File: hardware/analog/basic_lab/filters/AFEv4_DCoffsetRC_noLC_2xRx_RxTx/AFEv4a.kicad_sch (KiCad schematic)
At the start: 17 parts, among them J1 Connector_Generic_Conn_01x20, J2 Connector_Generic_Conn_01x02, J3 Connector_Generic_Conn_01x02, J4 Connector_Generic_Conn_01x02, J5 Connector_Generic_Conn_01x02, J6 Connector_Generic_Conn_01x02

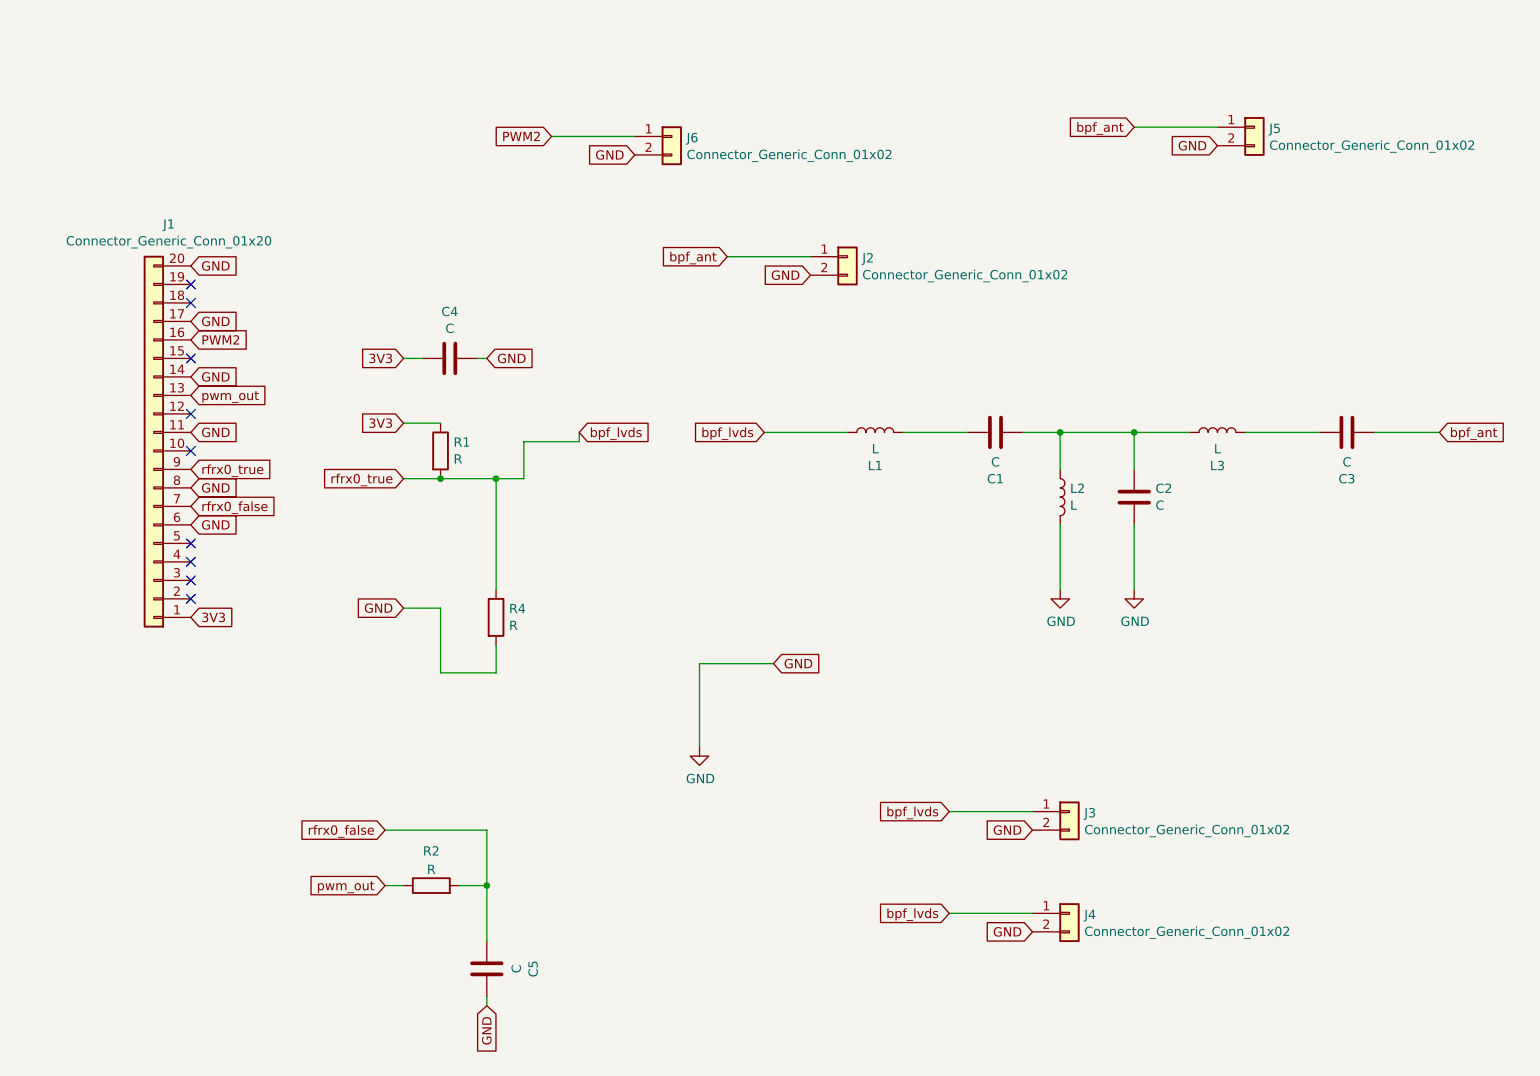
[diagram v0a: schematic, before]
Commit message: started 2xRx / RxTx PCBs with no / simple LC filters
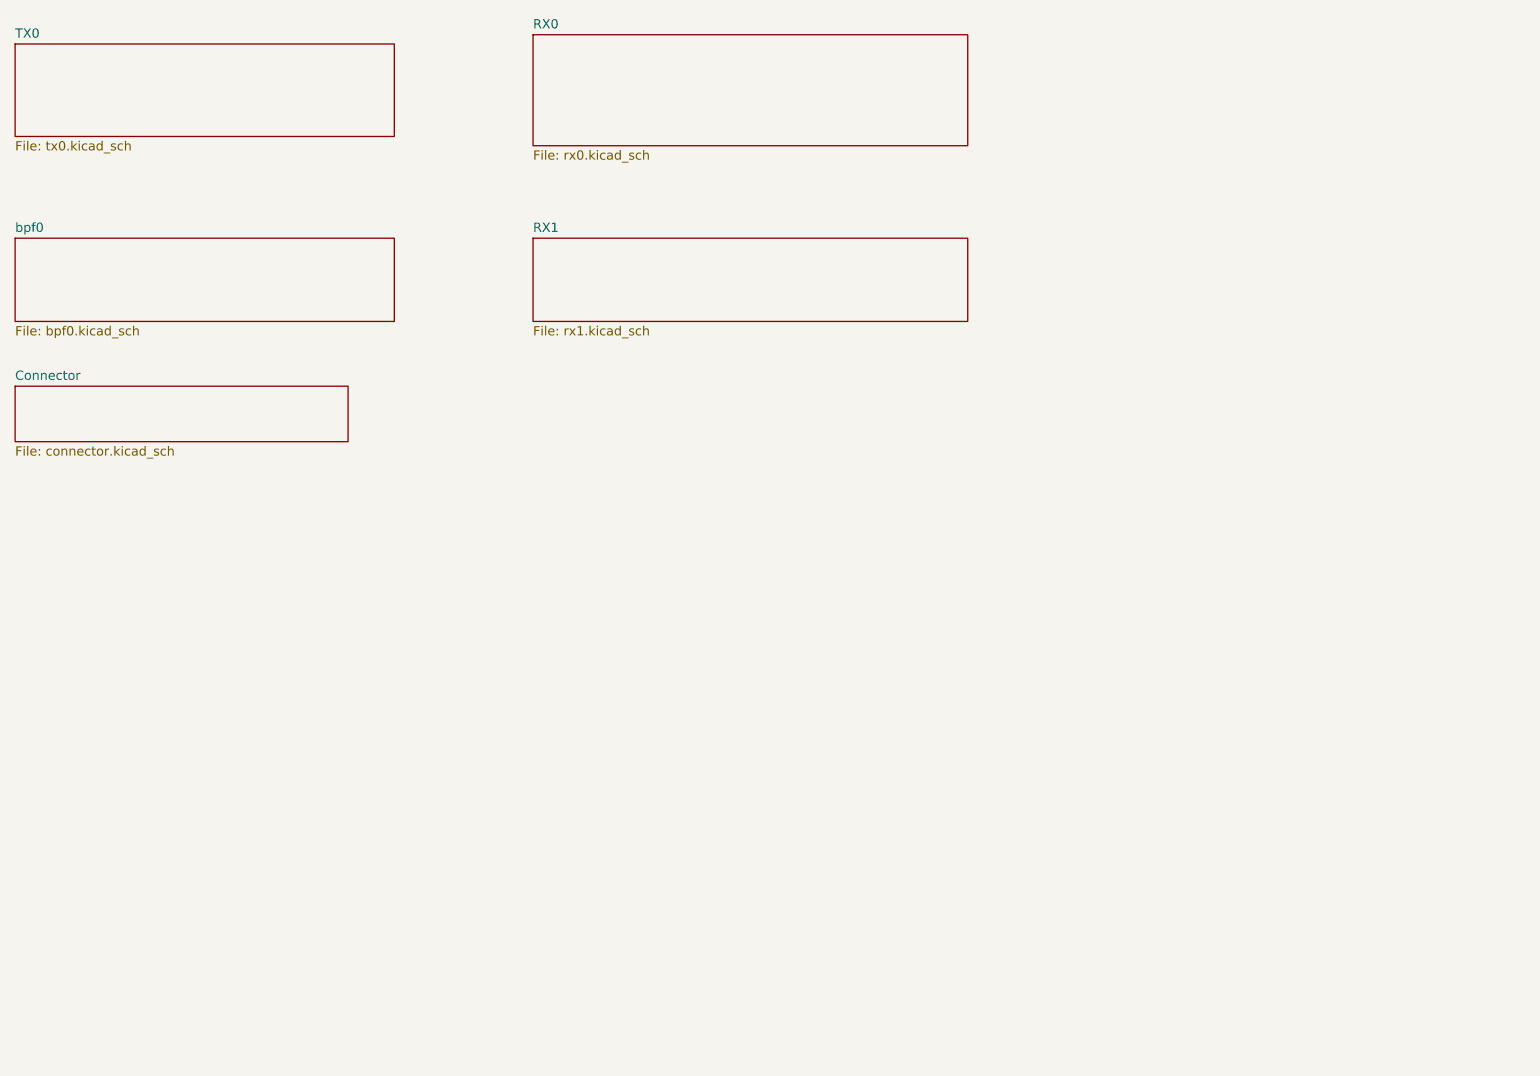
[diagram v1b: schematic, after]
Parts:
- removed C1, C2, C3, C4, C5: C, Capacitor_THT:C_Axial_L3.8mm_D2.6mm_P7.50mm_Horizontal, symbol Device:C
- removed J1: Connector_Generic_Conn_01x20, Connector_PinHeader_2.54mm:PinHeader_1x20_P2.54mm_Vertical, symbol bgt:Connector_Generic_Conn_01x20
- removed J2, J3, J4, J5, J6: Connector_Generic_Conn_01x02, Connector_PinHeader_2.54mm:PinHeader_1x02_P2.54mm_Vertical, symbol bgt:Connector_Generic_Conn_01x02
- removed L1, L2, L3: L, Inductor_THT:L_Toroid_Horizontal_D12.7mm_P20.00mm_Diameter14-5mm_Amidon-T50, symbol Device:L
- removed R1, R2, R4: R, Resistor_THT:R_Axial_DIN0207_L6.3mm_D2.5mm_P5.08mm_Vertical, symbol Device:R
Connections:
- no-connect marks 9 -> 0
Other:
- added sheet Connector (connector.kicad_sch)
- added sheet RX0 (rx0.kicad_sch)
- added sheet RX1 (rx1.kicad_sch)
- added sheet TX0 (tx0.kicad_sch)
- added sheet bpf0 (bpf0.kicad_sch)
